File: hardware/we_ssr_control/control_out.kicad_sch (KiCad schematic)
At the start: 12 parts

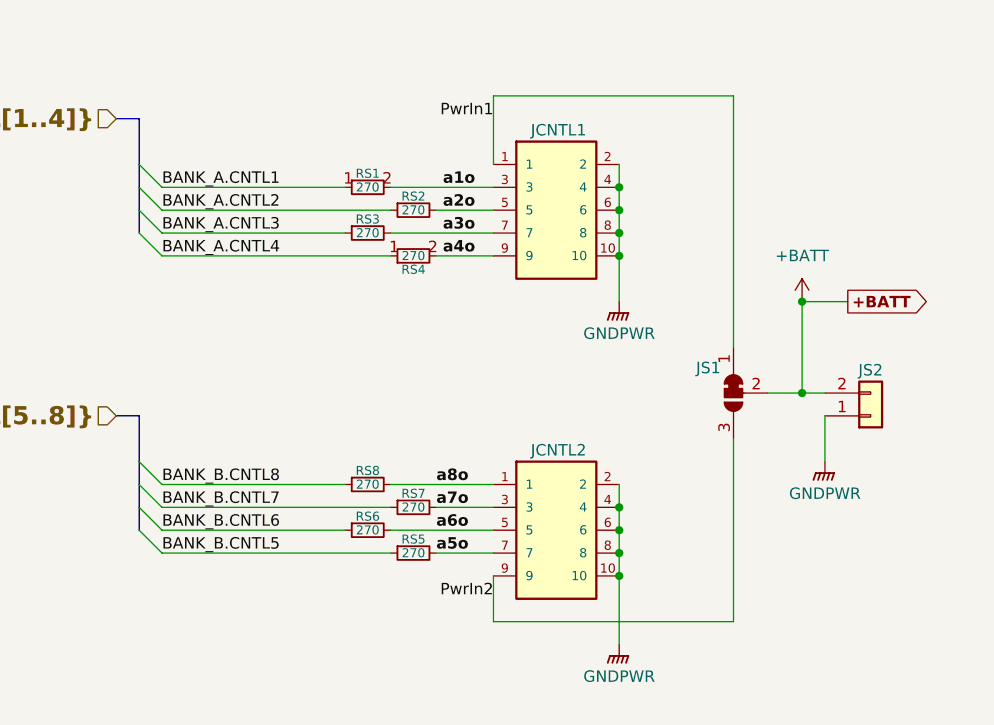
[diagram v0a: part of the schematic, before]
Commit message: Power supply changes plus misc.
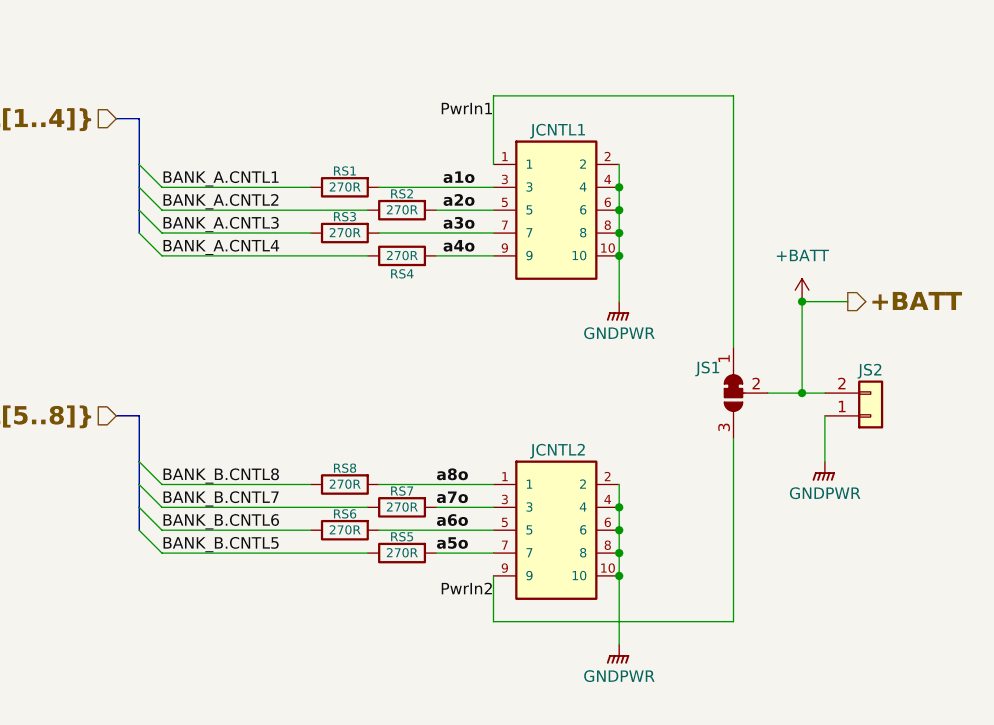
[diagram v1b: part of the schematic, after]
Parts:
- JCNTL1, JCNTL2: Characteristics (none) -> Headers & Wire Housings Shrouded Terminal Strip, 0.050"(1.2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; Package (none) -> Other
- JS2: footprint Connector_PinHeader_1.00mm:PinHeader_1x02_P1.00mm_Vertical -> dragon_mobile:PinHeader_1x02_P1.00mm_Vertical; Characteristics (none) -> Pin Header; 1mm 1x2 Vertical
- RS1, RS2, RS3, RS4, RS5, RS6, RS7, RS8: value 270 -> 270R; symbol Device:R_Small -> Device:R; Height (mm) (none) -> 0.45
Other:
- moved on the sheet: RS2, RS3, RS5, RS6, RS7, RS8

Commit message: Pre KiCad 7.0.0 WIP
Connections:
- net BANK_A.CNTL1 renamed BANK_A.OUT1
- net BANK_A.CNTL2 renamed BANK_A.OUT2
- net BANK_A.CNTL3 renamed BANK_A.OUT3
- net BANK_A.CNTL4 renamed BANK_A.OUT4
- net BANK_B.CNTL5 renamed BANK_B.OUT5
- net BANK_B.CNTL6 renamed BANK_B.OUT6
- net BANK_B.CNTL7 renamed BANK_B.OUT7
- net BANK_B.CNTL8 renamed BANK_B.OUT8
- net a1o renamed OUT1
- net a2o renamed OUT2
- net a3o renamed OUT3
- net a4o renamed OUT4
- net a5o renamed OUT5
- net a6o renamed OUT6
- net a7o renamed OUT7
- net a8o renamed OUT8
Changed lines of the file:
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@@
     (effects (font (size 1.27 1.27)) (justify left bottom))
   )
-  (label "a3o" (at 90.678 48.26 180)
-    (effects (font (size 1.27 1.27) (thickness 0.254) bold) (justify right bottom))
+  (label "OUT3" (at 86.36 48.26 0)
+    (effects (font (size 1.27 1.27) (thickness 0.254) bold) (justify left bottom))
   )
-  (label "BANK_B.CNTL8" (at 55.88 76.2 0)
+  (label "BANK_B.OUT8" (at 55.88 76.2 0)
     (effects (font (size 1.27 1.27)) (justify left bottom))
   )
-  (label "a6o" (at 86.36 81.28 0)
+  (label "OUT6" (at 86.36 81.28 0)
     (effects (font (size 1.27 1.27) bold) (justify left bottom))
   )
-  (label "BANK_A.CNTL2" (at 55.88 45.72 0)
+  (label "BANK_A.OUT2" (at 55.88 45.72 0)
     (effects (font (size 1.27 1.27)) (justify left bottom))
   )
-  (label "BANK_B.CNTL5" (at 55.88 83.82 0)
+  (label "BANK_B.OUT5" (at 55.88 83.82 0)
     (effects (font (size 1.27 1.27)) (justify left bottom))
   )
-  (label "BANK_A.CNTL4" (at 55.88 50.8 0)
+  (label "BANK_A.OUT4" (at 55.88 50.8 0)
     (effects (font (size 1.27 1.27)) (justify left bottom))
   )
-  (label "a4o" (at 90.678 50.8 180)
-    (effects (font (size 1.27 1.27) (thickness 0.254) bold) (justify right bottom))
+  (label "OUT4" (at 86.36 50.8 0)
+    (effects (font (size 1.27 1.27) (thickness 0.254) bold) (justify left bottom))
   )
-  (label "a8o" (at 86.36 76.2 0)
+  (label "OUT8" (at 86.36 76.2 0)
     (effects (font (size 1.27 1.27) bold) (justify left bottom))
   )
@@
     (effects (font (size 1.27 1.27)) (justify right bottom))
   )
-  (label "BANK_A.CNTL3" (at 55.88 48.26 0)
+  (label "BANK_A.OUT3" (at 55.88 48.26 0)
     (effects (font (size 1.27 1.27)) (justify left bottom))
   )
-  (label "BANK_B.CNTL6" (at 55.88 81.28 0)
+  (label "BANK_B.OUT6" (at 55.88 81.28 0)
     (effects (font (size 1.27 1.27)) (justify left bottom))
   )
-  (label "a7o" (at 86.36 78.74 0)
+  (label "OUT7" (at 86.36 78.74 0)
     (effects (font (size 1.27 1.27) bold) (justify left bottom))
   )
-  (label "BANK_B.CNTL7" (at 55.88 78.74 0)
+  (label "BANK_B.OUT7" (at 55.88 78.74 0)
     (effects (font (size 1.27 1.27)) (justify left bottom))
   )
-  (label "a5o" (at 86.36 83.82 0)
+  (label "OUT5" (at 86.36 83.82 0)
     (effects (font (size 1.27 1.27) bold) (justify left bottom))
   )
-  (label "BANK_A.CNTL1" (at 55.88 43.18 0)
+  (label "BANK_A.OUT1" (at 55.88 43.18 0)
     (effects (font (size 1.27 1.27)) (justify left bottom))
   )
@@
     (effects (font (size 1.27 1.27)) (justify right bottom))
   )
-  (label "a1o" (at 90.678 43.18 180)
-    (effects (font (size 1.27 1.27) (thickness 0.254) bold) (justify right bottom))
+  (label "OUT1" (at 86.36 43.18 0)
+    (effects (font (size 1.27 1.27) (thickness 0.254) bold) (justify left bottom))
   )
-  (label "a2o" (at 90.678 45.72 180)
-    (effects (font (size 1.27 1.27) (thickness 0.254) bold) (justify right bottom))
+  (label "OUT2" (at 86.36 45.72 0)
+    (effects (font (size 1.27 1.27) (thickness 0.254) bold) (justify left bottom))
   )
-  (hierarchical_label "BANK_B{CNTL[5..8]}" (shape input) (at 50.8 68.58 180)
+  (hierarchical_label "BANK_B{OUT[5..8]}" (shape input) (at 50.8 68.58 180)
     (effects (font (size 2 2) bold) (justify right))
   )
@@
     (effects (font (size 2 2) (thickness 0.4) bold) (justify left))
   )
-  (hierarchical_label "BANK_A{CNTL[1..4]}" (shape input) (at 50.8 35.56 180)
+  (hierarchical_label "BANK_A{OUT[1..4]}" (shape input) (at 50.8 35.56 180)
     (effects (font (size 2 2) bold) (justify right))
   )
